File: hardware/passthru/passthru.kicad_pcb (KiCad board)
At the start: 2 copper layers, 63.5 x 59.7 mm, 83 parts, among them J1 ARM_SWD, J2 RJ45_LED_Shielded, J3 Screw_Terminal_01x02, Q1 Q_PMOS_DGS, Q2 Q_PMOS_DGS, Q3 Q_NPN_BEC, U1 EFM32GG11B8xx, U2 KSZ8081RND, U3 LM5085, U4 TPS2375-1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

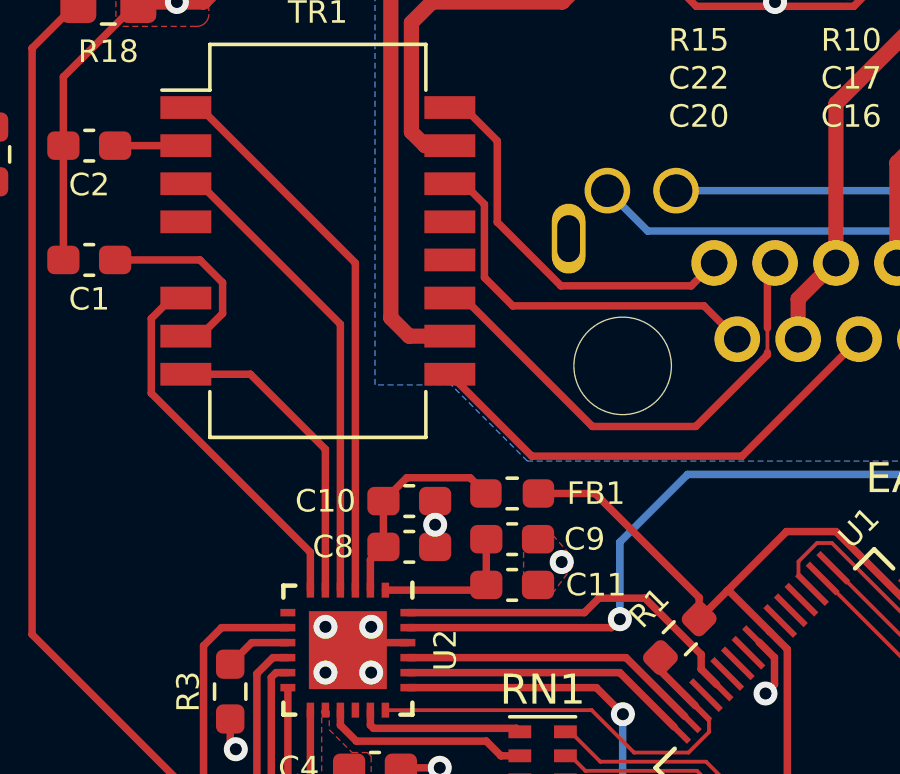
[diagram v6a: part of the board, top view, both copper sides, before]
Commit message: passthru: rebalance RX/TX pairs
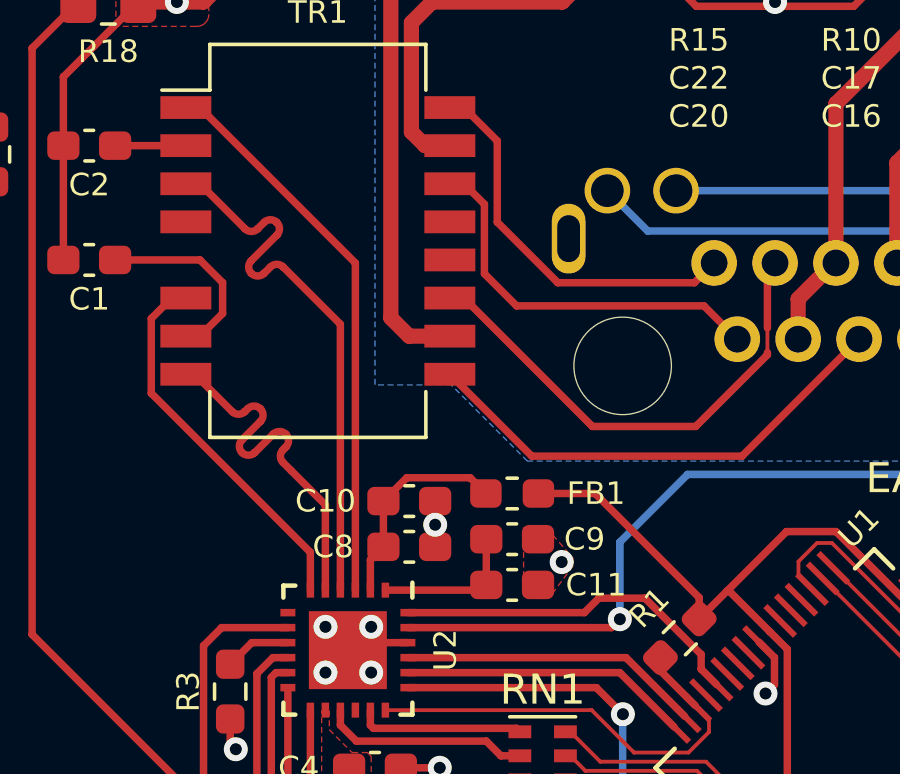
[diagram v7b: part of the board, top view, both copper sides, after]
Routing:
- net /ETH_RX+: track 15.5 -> 18.2 mm
- net /ETH_TX-: track 10.4 -> 12.6 mm
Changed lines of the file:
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@@
   (segment (start 156.9878 77.3537) (end 156.9878 85.2073) (width 0.25) (layer "F.Cu") (net 11))
   (segment (start 149.7381 70.104) (end 156.9878 77.3537) (width 0.25) (layer "F.Cu") (net 11))
+  (segment (start 142.75 93.789) (end 142.0912 94.4478) (width 0.25) (layer "F.Cu") (net 12))
+  (segment (start 142.0912 94.4478) (end 137.541208 94.4478) (width 0.25) (layer "F.Cu") (net 12))
   (segment (start 135.520101 89.718701) (end 134.41 88.6086) (width 0.25) (layer "F.Cu") (net 12))
-  (segment (start 142.75 93.789) (end 141.988001 94.550999) (width 0.25) (layer "F.Cu") (net 12))
+  (segment (start 137.541208 94.4478) (end 135.520101 92.426693) (width 0.25) (layer "F.Cu") (net 12))
   (segment (start 135.520101 92.426693) (end 135.520101 89.718701) (width 0.25) (layer "F.Cu") (net 12))
-  (segment (start 141.988001 94.550999) (end 137.644407 94.550999) (width 0.25) (layer "F.Cu") (net 12))
-  (segment (start 137.644407 94.550999) (end 135.520101 92.426693) (width 0.25) (layer "F.Cu") (net 12))
-  (segment (start 136.036799 95.218999) (end 142.409999 95.218999) (width 0.25) (layer "F.Cu") (net 13))
+  (segment (start 135.0928 91.8314) (end 135.0928 94.148) (width 0.25) (layer "F.Cu") (net 13))
+  (segment (start 135.0928 94.148) (end 136.163799 95.218999) (width 0.25) (layer "F.Cu") (net 13))
+  (segment (start 134.41 91.1486) (end 135.0928 91.8314) (width 0.25) (layer "F.Cu") (net 13))
   (segment (start 142.409999 95.218999) (end 143.52 96.329) (width 0.25) (layer "F.Cu") (net 13))
-  (segment (start 135.0928 94.275) (end 136.036799 95.218999) (width 0.25) (layer "F.Cu") (net 13))
-  (segment (start 134.41 91.1486) (end 135.0928 91.8314) (width 0.25) (layer "F.Cu") (net 13))
-  (segment (start 135.0928 91.8314) (end 135.0928 94.275) (width 0.25) (layer "F.Cu") (net 13))
+  (segment (start 136.163799 95.218999) (end 142.409999 95.218999) (width 0.25) (layer "F.Cu") (net 13))
   (segment (start 142.1374 99.2388) (end 138.6902 99.2388) (width 0.25) (layer "F.Cu") (net 14))
   (segment (start 138.6902 99.2388) (end 134.41 94.9586) (width 0.25) (layer "F.Cu") (net 14))
@@
   (segment (start 141.864102 100.838) (end 139.606931 103.095171) (width 0.25) (layer "B.Cu") (net 16))
   (segment (start 139.606931 103.095171) (end 139.606931 105.664) (width 0.25) (layer "B.Cu") (net 16))
-  (segment (start 125.14 97.4986) (end 127.2924 97.4986) (width 0.25) (layer "F.Cu") (net 17))
-  (segment (start 129.791 99.9972) (end 127.2924 97.4986) (width 0.25) (layer "F.Cu") (net 17))
-  (segment (start 129.791 104.695) (end 129.791 99.9972) (width 0.25) (layer "F.Cu") (net 17))
+  (segment (start 128.473732 99.921113) (end 128.379553 100.015289) (width 0.25) (layer "F.Cu") (net 17))
+  (segment (start 127.43685 100.109467) (end 127.436849 100.109468) (width 0.25) (layer "F.Cu") (net 17))
+  (segment (start 125.14 97.4986) (end 125.4386 97.4986) (width 0.25) (layer "F.Cu") (net 17))
+  (segment (start 127.106765 98.742499) (end 127.106764 98.7425) (width 0.25) (layer "F.Cu") (net 17))
+  (segment (start 127.436849 100.109468) (end 128.049466 99.496847) (width 0.25) (layer "F.Cu") (net 17))
+  (segment (start 125.4386 97.4986) (end 126.6825 98.7425) (width 0.25) (layer "F.Cu") (net 17))
+  (segment (start 127.625205 99.072588) (end 127.625206 99.072587) (width 0.25) (layer "F.Cu") (net 17))
+  (segment (start 128.660307 100.720307) (end 129.791 101.851) (width 0.25) (layer "F.Cu") (net 17))
+  (segment (start 129.791 101.851) (end 129.791 104.695) (width 0.25) (layer "F.Cu") (net 17))
+  (segment (start 127.106764 98.7425) (end 127.200942 98.648323) (width 0.25) (layer "F.Cu") (net 17))
+  (segment (start 127.625206 99.072587) (end 127.012585 99.685204) (width 0.25) (layer "F.Cu") (net 17))
+  (segment (start 128.379553 100.439553) (end 128.660307 100.720307) (width 0.25) (layer "F.Cu") (net 17))
+  (segment (start 128.473731 99.921114) (end 128.473732 99.921113) (width 0.25) (layer "F.Cu") (net 17))
+  (arc (start 127.012585 99.685204) (mid 126.924717 99.897336) (end 127.012585 100.109468) (width 0.25) (layer "F.Cu") (net 17))
+  (arc (start 128.049466 99.496847) (mid 128.2616 99.408981) (end 128.473732 99.496849) (width 0.25) (layer "F.Cu") (net 17))
+  (arc (start 127.200942 98.648323) (mid 127.413074 98.560455) (end 127.625206 98.648323) (width 0.25) (layer "F.Cu") (net 17))
+  (arc (start 126.6825 98.7425) (mid 126.894634 98.830369) (end 127.106765 98.742499) (width 0.25) (layer "F.Cu") (net 17))
+  (arc (start 127.012585 100.109468) (mid 127.224718 100.197336) (end 127.43685 100.109467) (width 0.25) (layer "F.Cu") (net 17))
+  (arc (start 128.379553 100.015289) (mid 128.291685 100.227421) (end 128.379553 100.439553) (width 0.25) (layer "F.Cu") (net 17))
+  (arc (start 127.625206 98.648323) (mid 127.713073 98.860455) (end 127.625205 99.072588) (width 0.25) (layer "F.Cu") (net 17))
+  (arc (start 128.473732 99.496849) (mid 128.561599 99.708981) (end 128.473731 99.921114) (width 0.25) (layer "F.Cu") (net 17))
   (segment (start 122.7825 93.6886) (end 125.61 93.6886) (width 0.25) (layer "F.Cu") (net 18))
   (segment (start 125.61 96.2286) (end 126.365 95.4736) (width 0.25) (layer "F.Cu") (net 18))
@@
   (segment (start 129.291 104.695) (end 129.291 103.4352) (width 0.25) (layer "F.Cu") (net 19))
   (segment (start 129.291 103.4352) (end 123.9872 98.1314) (width 0.25) (layer "F.Cu") (net 19))
-  (segment (start 125.61 91.1486) (end 130.291 95.8296) (width 0.25) (layer "F.Cu") (net 20))
   (segment (start 130.291 95.8296) (end 130.291 104.695) (width 0.25) (layer "F.Cu") (net 20))
+  (segment (start 127.535364 92.6497) (end 127.747497 92.437568) (width 0.25) (layer "F.Cu") (net 20))
+  (segment (start 127.747494 94.134623) (end 127.959626 93.92249) (width 0.25) (layer "F.Cu") (net 20))
+  (segment (start 127.535365 92.649699) (end 127.535364 92.6497) (width 0.25) (layer "F.Cu") (net 20))
+  (segment (start 125.61 91.1486) (end 127.1111 92.6497) (width 0.25) (layer "F.Cu") (net 20))
+  (segment (start 128.171762 92.437569) (end 128.171761 92.437568) (width 0.25) (layer "F.Cu") (net 20))
+  (segment (start 128.383891 93.922491) (end 128.38389 93.92249) (width 0.25) (layer "F.Cu") (net 20))
+  (segment (start 128.17176 92.861833) (end 128.171761 92.861832) (width 0.25) (layer "F.Cu") (net 20))
+  (segment (start 128.171761 92.861832) (end 127.32323 93.710359) (width 0.25) (layer "F.Cu") (net 20))
+  (segment (start 128.38389 93.92249) (end 130.291 95.8296) (width 0.25) (layer "F.Cu") (net 20))
+  (segment (start 127.747495 94.134622) (end 127.747494 94.134623) (width 0.25) (layer "F.Cu") (net 20))
+  (arc (start 127.1111 92.6497) (mid 127.323234 92.737569) (end 127.535365 92.649699) (width 0.25) (layer "F.Cu") (net 20))
+  (arc (start 127.32323 93.710359) (mid 127.235362 93.922491) (end 127.32323 94.134623) (width 0.25) (layer "F.Cu") (net 20))
+  (arc (start 127.32323 94.134623) (mid 127.535363 94.222491) (end 127.747495 94.134622) (width 0.25) (layer "F.Cu") (net 20))
+  (arc (start 127.959626 93.92249) (mid 128.171759 93.834622) (end 128.383891 93.922491) (width 0.25) (layer "F.Cu") (net 20))
+  (arc (start 128.171761 92.437568) (mid 128.259628 92.6497) (end 128.17176 92.861833) (width 0.25) (layer "F.Cu") (net 20))
+  (arc (start 127.747497 92.437568) (mid 127.959629 92.349699) (end 128.171762 92.437569) (width 0.25) (layer "F.Cu") (net 20))
   (segment (start 125.14 89.8786) (end 122.7825 89.8786) (width 0.25) (layer "F.Cu") (net 21))
   (segment (start 130.791 104.695) (end 130.791 93.7896) (width 0.25) (layer "F.Cu") (net 22))
